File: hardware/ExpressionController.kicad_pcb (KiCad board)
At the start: 2 copper layers, 86.6 x 72.6 mm, 130 parts, among them J1 DC, J2 Exp1, J3 Exp2, J4 Exp3, J5 Exp4, Q1 DMP3099L-7, U1 ADP7142AUJZ-3.3, U10 74HC595, U12 74HC595, U14 74AHCT1G125, U15 TMUX1511PWR, U16 TMUX1511PWR, U17 TMUX1511PWR, U18 TMUX1511PWR, U19 TMUX1511PWR, U2 ADP7142AUJZ-5.0, U20 TMUX1511PWR, U21 TMUX1511PWR, U22 TMUX1511PWR, U3 ADP7142AUJZ-2.5, U4 AD7718, U5 AD7718, U6 74HC595, U8 74HC595, Y1 MS1V-T1K-32.768kHz-12.5pF-20P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, Y2 MS1V-T1K-32.768kHz-12.5pF-20P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

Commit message: added mouser part numbers
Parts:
- C17: footprint Capacitor_SMD:C_1210_3225Metric -> Capacitor_SMD:C_0805_2012Metric
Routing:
- net Net-(U16-SEL2): track 25.8 -> 25.2 mm

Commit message: added all footprints and parts
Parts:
- J1: value DC -> BarrelJack
- J2: value Exp1 -> AudioJack
- J3: value Exp2 -> AudioJack
- J4: value Exp3 -> AudioJack
- J5: value Exp4 -> AudioJack
- R50, R51, R52, R53, R54, R55, R56, R57: value 1k -> 1k 0.1%
- U10, U12, U6, U8: value 74HC595 -> 74HC595DR; footprint Package_SO:SOIC-16W_7.5x10.3mm_P1.27mm -> Package_SO:SOIC-16_3.9x9.9mm_P1.27mm
- U4, U5: value AD7718 -> AD7718BRZ
- Y1, Y2: value MS1V-T1K-32.768kHz-12.5pF-20PPM-TA-QC-Au -> 32.768kHz; footprint Crystal:Crystal_SMD_3215-2Pin_3.2x1.5mm -> MS1V-T1K:MS1V-T1K
- turned Y1 to -90 degrees
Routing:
- net Net-(C15-Pad1): track 9.66 -> 0.00 mm
- net Net-(U4-XTAL1): track 6.98 -> 0.00 mm

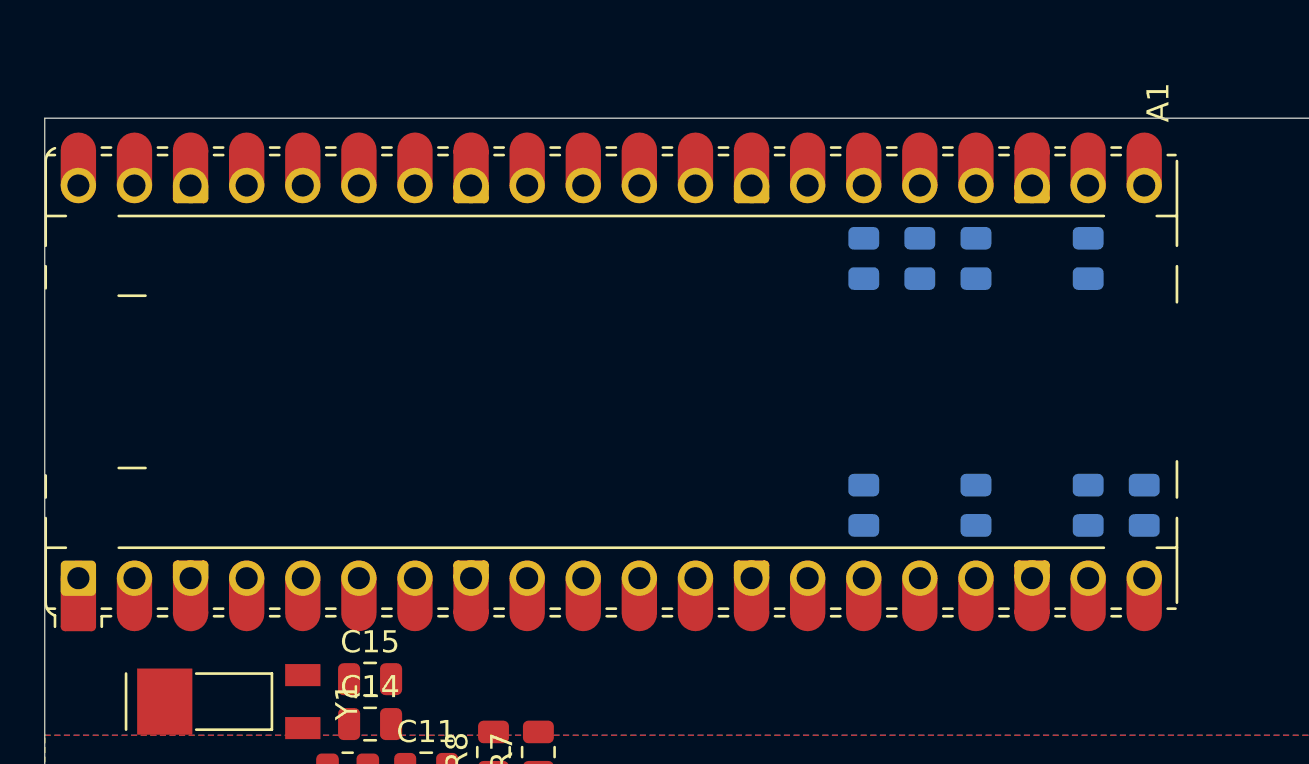
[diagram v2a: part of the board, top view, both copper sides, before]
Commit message: updated Pico footprint
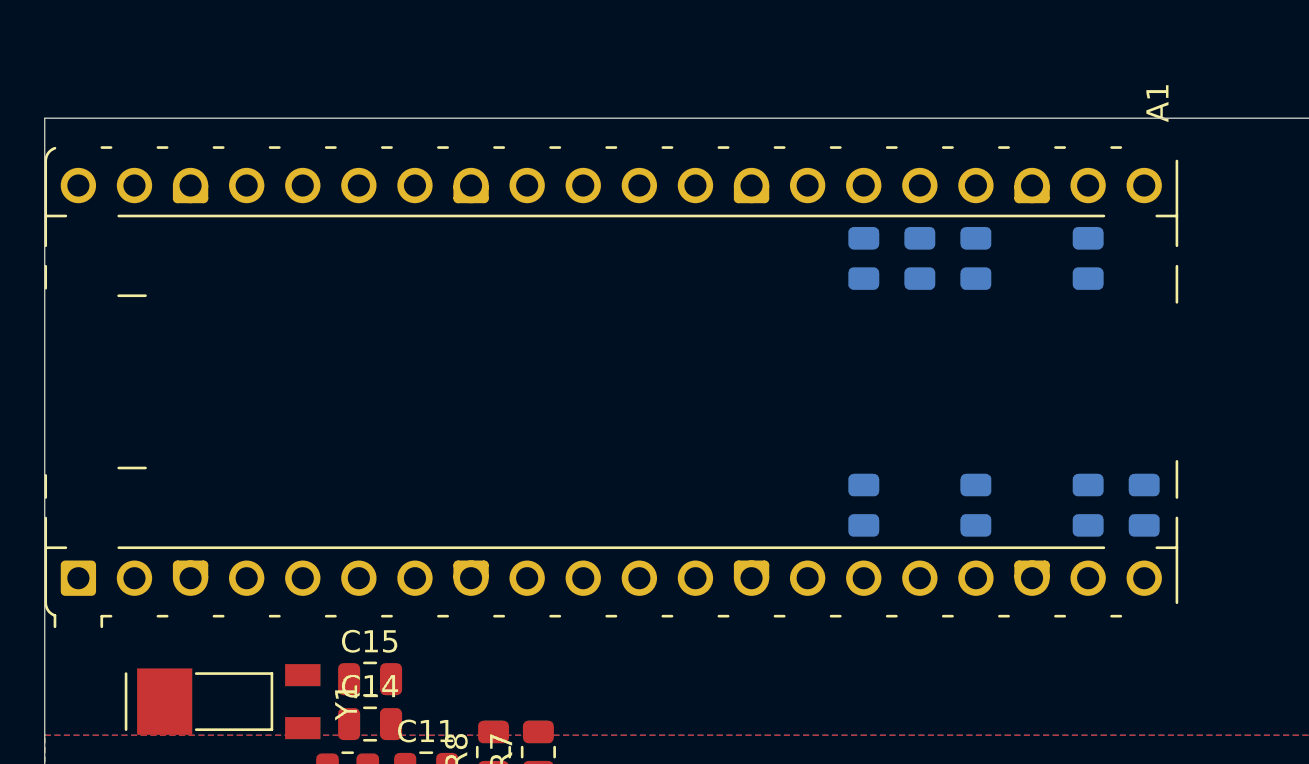
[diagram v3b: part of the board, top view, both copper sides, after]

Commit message: more routing
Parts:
- C14, C15, Y1: moved to B.Cu
- moved C50 96.5 mm to (147.1, 186.2), turned to 0 degrees
- moved Y1 7.92 mm to (135.3, 152.4)
- moved C40 6.19 mm to (152.1, 186.2), turned to 180 degrees
- moved C41 6.19 mm to (194.8, 186.2), turned to 180 degrees
- moved C42 6.19 mm to (173.5, 186.2), turned to 180 degrees
- moved C39 6.19 mm to (130.8, 186.2), turned to 180 degrees
- moved C14 4.33 mm to (131.8, 153.7), turned to 180 degrees
- moved C49 4.32 mm to (125.7, 186.2), turned to 0 degrees
- moved C15 3.82 mm to (131.8, 151.1), turned to 180 degrees
- moved C54 1.98 mm to (156.0, 165.9)
- moved C58 1.98 mm to (156.0, 171.4)
- moved R44 1.85 mm to (131.1, 149.6), turned to 90 degrees
- moved U10 1.78 mm to (170.9, 180.3)
- moved U12 1.78 mm to (192.3, 180.3)
- moved U6 1.78 mm to (128.3, 180.3)
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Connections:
- Y1 pad 1: Net-(C15-Pad1) -> Net-(U4-XTAL1)
- Y1 pad 2: Net-(U4-XTAL1) -> Net-(C15-Pad1)
- Y2 pad 1: Net-(C22-Pad1) -> Net-(U5-XTAL1)
- Y2 pad 2: Net-(U5-XTAL1) -> Net-(C22-Pad1)
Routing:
- net SR_CLK: track 0.00 -> 108.5 mm, vias 0 -> 4
- net SR_LAT: track 0.00 -> 107.7 mm, vias 0 -> 4
- net SR_OE: track 0.00 -> 99.1 mm, vias 0 -> 4
- net /AnalogFrontend/AnalogQuadChannel2/DRIVE_DO: track 0.00 -> 29.9 mm, vias 0 -> 2
- net /AnalogFrontend/AnalogQuadChannel3/DRIVE_DO: track 0.00 -> 29.9 mm, vias 0 -> 2
- net /AnalogFrontend/AnalogQuadChannel1/DRIVE_DO: track 0.00 -> 29.9 mm, vias 0 -> 2
- net Net-(D5-DOUT): track 0.00 -> 17.8 mm
- net Net-(D4-DOUT): track 0.00 -> 17.8 mm
- net Net-(D6-DOUT): track 0.00 -> 17.8 mm
- net +5V: track 0.00 -> 15.4 mm
- net +3.3VA: track 26.1 -> 39.1 mm
- net +2.5V: track 80.4 -> 71.0 mm
- net Net-(U4-XTAL1): track 0.00 -> 9.39 mm, vias 0 -> 1
- net Net-(C15-Pad1): track 0.00 -> 7.32 mm, vias 0 -> 1
- net /AnalogFrontend/AnalogQuadChannel2/JACK4: track 16.8 -> 22.8 mm
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
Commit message: more routing of input 3 and 4
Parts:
- C13, C20, C21, C22, C55, C56, Y2: moved to B.Cu
- moved R52 126.0 mm to (170.9, 161.8), turned to -90 degrees
- moved C59 124.0 mm to (177.3, 171.4), turned to 90 degrees
- moved C56 91.5 mm to (198.6, 165.9), turned to 90 degrees
- moved R53 90.5 mm to (192.3, 161.8), turned to -90 degrees
- moved C60 90.3 mm to (198.6, 171.4), turned to 90 degrees
- moved C51 89.4 mm to (168.4, 186.2), turned to 0 degrees
- moved C20 89.1 mm to (181.6, 161.8), turned to -90 degrees
- moved C52 88.9 mm to (189.7, 186.2), turned to 0 degrees
- moved C17 86.4 mm to (178.1, 168.1)
- moved C16 85.8 mm to (178.1, 165.9)
- moved R10 85.5 mm to (180.3, 149.6)
- moved R9 85.2 mm to (182.9, 149.6)
- moved C18 85.2 mm to (177.0, 150.4)
- moved R45 84.8 mm to (173.7, 149.6)
- moved C21 81.6 mm to (174.5, 153.7)
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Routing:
- net +3.3VA: track 39.1 -> 268.3 mm, vias 2 -> 20
- net /AnalogFrontend/AnalogQuadChannel4/JACK3: track 0.00 -> 36.2 mm, vias 0 -> 4
- net /AnalogFrontend/AnalogQuadChannel3/JACK3: track 0.00 -> 36.1 mm, vias 0 -> 4
- net /AnalogFrontend/AnalogQuadChannel3/ADC4: track 2.20 -> 32.5 mm
- net /AnalogFrontend/AnalogQuadChannel3/JACK2: track 0.00 -> 30.2 mm, vias 0 -> 4
- net /AnalogFrontend/AnalogQuadChannel4/ADC1: track 0.00 -> 29.6 mm
- net /AnalogFrontend/AnalogQuadChannel4/JACK2: track 0.00 -> 27.5 mm, vias 0 -> 4
- net /AnalogFrontend/AnalogQuadChannel4/JACK1: track 0.00 -> 25.7 mm, vias 0 -> 4
- net /AnalogFrontend/AnalogQuadChannel3/JACK1: track 0.00 -> 23.9 mm, vias 0 -> 4
- net /AnalogFrontend/AnalogQuadChannel4/JACK4: track 0.00 -> 22.8 mm, vias 0 -> 4
- net Net-(U10-QA): track 0.00 -> 22.0 mm
- net /AnalogFrontend/AnalogQuadChannel3/JACK4: track 0.00 -> 21.9 mm, vias 0 -> 4
- net Net-(U12-QA): track 0.00 -> 21.7 mm
- net Net-(U10-QG): track 0.00 -> 21.5 mm
- net Net-(U12-QG): track 0.00 -> 21.2 mm
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
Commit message: more routing progress
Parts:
- removed R59: 47, Resistor_SMD:R_0805_2012Metric
- D3, R58: moved to B.Cu
- moved R56 135.6 mm to (164.3, 172.0), turned to 180 degrees
- moved R58 124.2 mm to (153.9, 148.6), turned to -90 degrees
- moved R43 118.7 mm to (120.1, 152.4), turned to 180 degrees
- moved U14 114.8 mm to (124.0, 152.4)
- moved C48 114.5 mm to (124.2, 150.1)
- moved R57 101.0 mm to (185.7, 172.0), turned to 180 degrees
- moved C8 83.3 mm to (171.2, 144.0), turned to -90 degrees
- moved U3 76.3 mm to (175.0, 142.0), turned to 180 degrees
- moved D3 49.8 mm to (173.5, 127.5), turned to 0 degrees
- moved C2 48.3 mm to (185.7, 136.4), turned to 90 degrees
- moved R1 48.0 mm to (172.7, 130.0), turned to -90 degrees
- moved D2 44.2 mm to (176.5, 130.0)
- moved C4 33.8 mm to (178.8, 144.0), turned to -90 degrees
- moved C1 33.1 mm to (177.0, 136.1), turned to 180 degrees
- moved D1 30.4 mm to (185.4, 129.8)
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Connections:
- A1 pad 16: SR_WB -> unconnected-(A1-GPIO12-Pad16)
- R58 pad 1: SR_OE -> Net-(A1-GPIO11)
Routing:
- net +5V: track 15.4 -> 235.8 mm, vias 0 -> 2
- net SR_DATA: track 0.00 -> 105.0 mm, vias 0 -> 2
- net SR_CLK: track 108.5 -> 205.6 mm, vias 4 -> 5
- net SR_LAT: track 107.7 -> 200.8 mm, vias 4 -> 5
- net SR_OE: track 99.1 -> 188.8 mm, vias 4 -> 5
- net SPI0_CLK: track 0.00 -> 74.9 mm, vias 0 -> 1
- net SPI0_TX: track 0.00 -> 71.5 mm, vias 0 -> 1
- net SPI0_NRDY2: track 0.00 -> 53.3 mm
- net PICO_VSYS: track 0.00 -> 52.7 mm
- net SPI0_NCS2: track 0.00 -> 51.2 mm, vias 0 -> 1
- net SPI0_NCS1: track 0.00 -> 46.0 mm, vias 0 -> 1
- net Net-(D4-DIN): track 0.00 -> 44.2 mm
- net SPI0_RX: track 0.00 -> 42.6 mm
- net +3.3VA: track 268.3 -> 306.2 mm, vias 20 -> 24
- net +2.5V: track 74.0 -> 107.9 mm, vias 4 -> 8
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- added copper zone on F.Cu, net +2.5V
- added copper zone on F.Cu, net +3.3VA
- added copper zone on F.Cu, net +5V
- added copper zone on F.Cu, net Net-(C47-Pad1)
- added copper zone on F.Cu, net Net-(D1-A1)
- added copper zone on F.Cu, net VEXT
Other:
- board size 86.6 x 72.6 mm -> 88.6 x 69.8 mm

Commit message: everything except ground connected
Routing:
- net +3.3VA: track 306.2 -> 385.9 mm, vias 24 -> 29
- net SPI0_RX: track 42.6 -> 66.0 mm, vias 0 -> 1
- net Net-(U15-SEL2): track 22.0 -> 32.5 mm
- net Net-(A1-GPIO20): track 0.00 -> 2.39 mm
- net Net-(A1-GPIO19): track 0.00 -> 2.39 mm
- net Net-(A1-GPIO18): track 0.00 -> 2.39 mm
- net Net-(A1-GPIO17): track 0.00 -> 2.39 mm
- net SPI0_CLK: track 74.9 -> 76.5 mm
- net SPI0_NCS1: track 46.0 -> 47.4 mm
- net +2.5V: track 107.9 -> 107.1 mm
- net /AnalogFrontend/AnalogQuadChannel3/ADC2: track 20.0 -> 20.8 mm

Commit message: nightly progress
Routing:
- net GND: track 23.0 -> 29.9 mm, vias 68 -> 159
- net +3.3VA: track 385.9 -> 384.4 mm, vias 29 -> 24
- net /AnalogFrontend/AnalogQuadChannel4/JACK1: track 25.7 -> 24.2 mm, vias 4 -> 2
- net /AnalogFrontend/AnalogQuadChannel2/JACK1: track 25.7 -> 24.6 mm
- net SPI0_TX: track 71.5 -> 70.7 mm
- net +2.5V: track 107.1 -> 106.5 mm
- net Net-(U5-XTAL1): track 9.39 -> 9.18 mm, vias 2 -> 1
- net /AnalogFrontend/AnalogQuadChannel4/JACK4: vias 4 -> 2
- net /AnalogFrontend/AnalogQuadChannel4/JACK3: vias 4 -> 2
- net /AnalogFrontend/AnalogQuadChannel4/JACK2: vias 4 -> 1
- net /AnalogFrontend/AnalogQuadChannel3/JACK4: vias 4 -> 2
- net /AnalogFrontend/AnalogQuadChannel3/JACK3: vias 4 -> 2
- net /AnalogFrontend/AnalogQuadChannel3/JACK2: vias 4 -> 2
- net /AnalogFrontend/AnalogQuadChannel3/JACK1: vias 4 -> 2
- net /AnalogFrontend/AnalogQuadChannel2/JACK2: vias 2 -> 1
